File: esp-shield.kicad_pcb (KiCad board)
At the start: 2 copper layers, 53.5 x 52.5 mm, 23 parts, among them J1 Conn_02x03_Counter_Clockwise, J2 Conn_01x08, J3 Conn_01x06, J4 Conn_01x08, SW1 RESET, SW2 PROG, U2 ESP-01

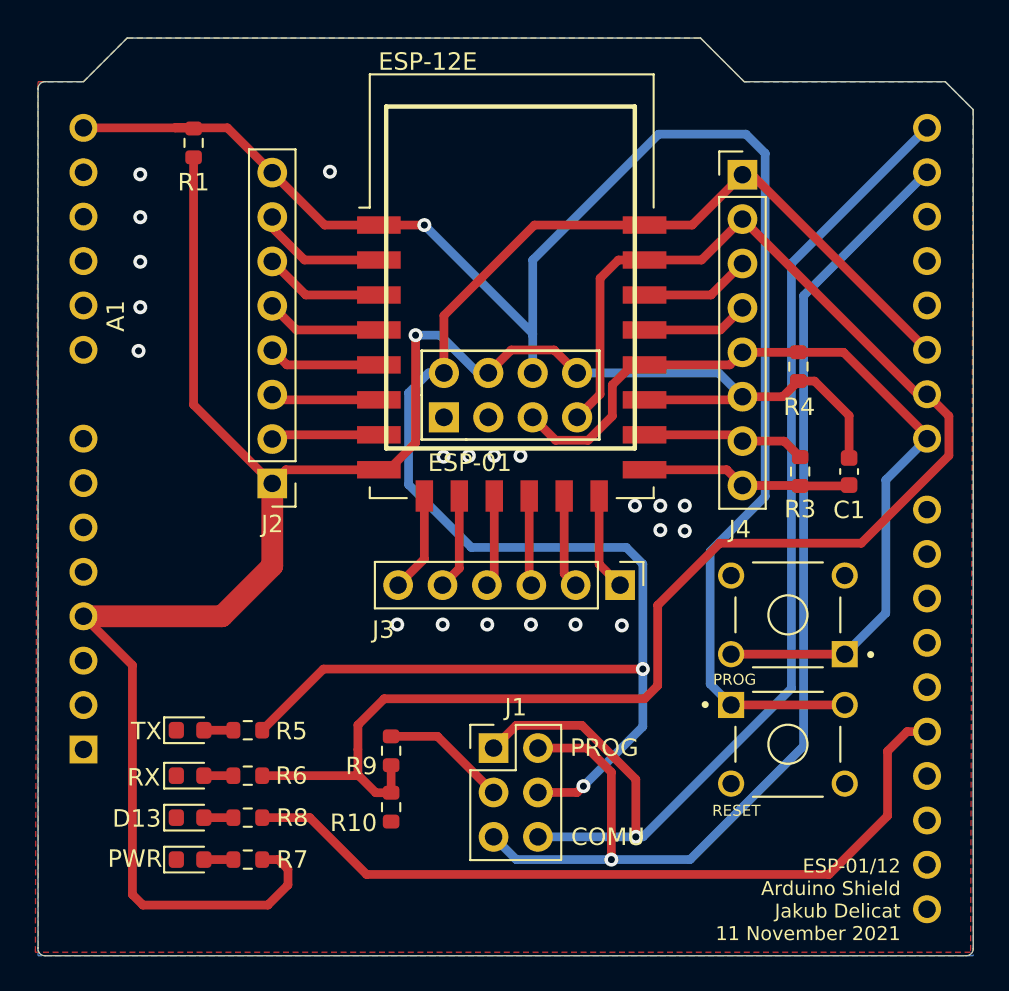
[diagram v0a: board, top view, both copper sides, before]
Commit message: Added esp112E labeling
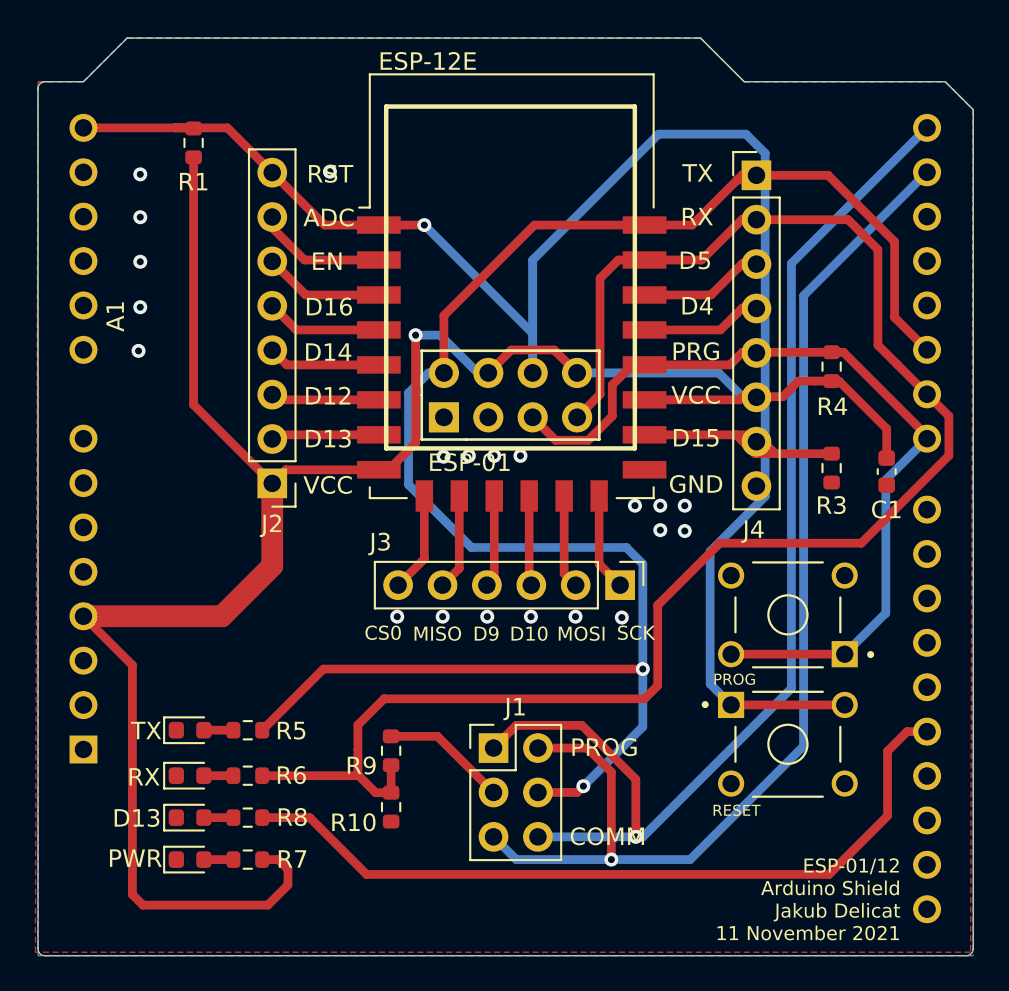
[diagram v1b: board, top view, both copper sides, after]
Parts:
- moved C1 2.15 mm to (101.0, 44.5)
- moved R4 1.90 mm to (97.8, 38.5)
- moved R3 1.81 mm to (97.8, 44.3)
- moved J4 0.80 mm to (93.5, 27.6)
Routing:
- net GND: track 12.1 -> 0.21 mm
- net GPIO15: track 9.43 -> 13.9 mm
- net RX_PROG: track 91.9 -> 95.9 mm
- net TX_PROG: track 101.7 -> 105.2 mm
- net VCC: track 118.5 -> 120.7 mm
- net GPIO4: track 6.12 -> 6.94 mm
- net GPIO5: track 6.35 -> 7.16 mm
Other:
- board text added: "ADC"
- board text added: "COMM"
- board text added: "CS0"
- board text added: "D10"
- board text added: "D12"
- board text added: "D13"
- board text added: "D14"
- board text added: "D15"
- board text added: "D16"
- board text added: "D4"
- board text added: "D5"
- board text added: "D9"
- board text added: "EN"
- board text added: "GND"
- board text added: "MISO"
- board text added: "MOSI"
- board text added: "PRG"
- board text added: "RST"
- board text added: "RX"
- board text added: "SCK"
- board text added: "TX"
- board text added: "VCC"
- board text removed: "COMU"

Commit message: Added Arduino pinout labels
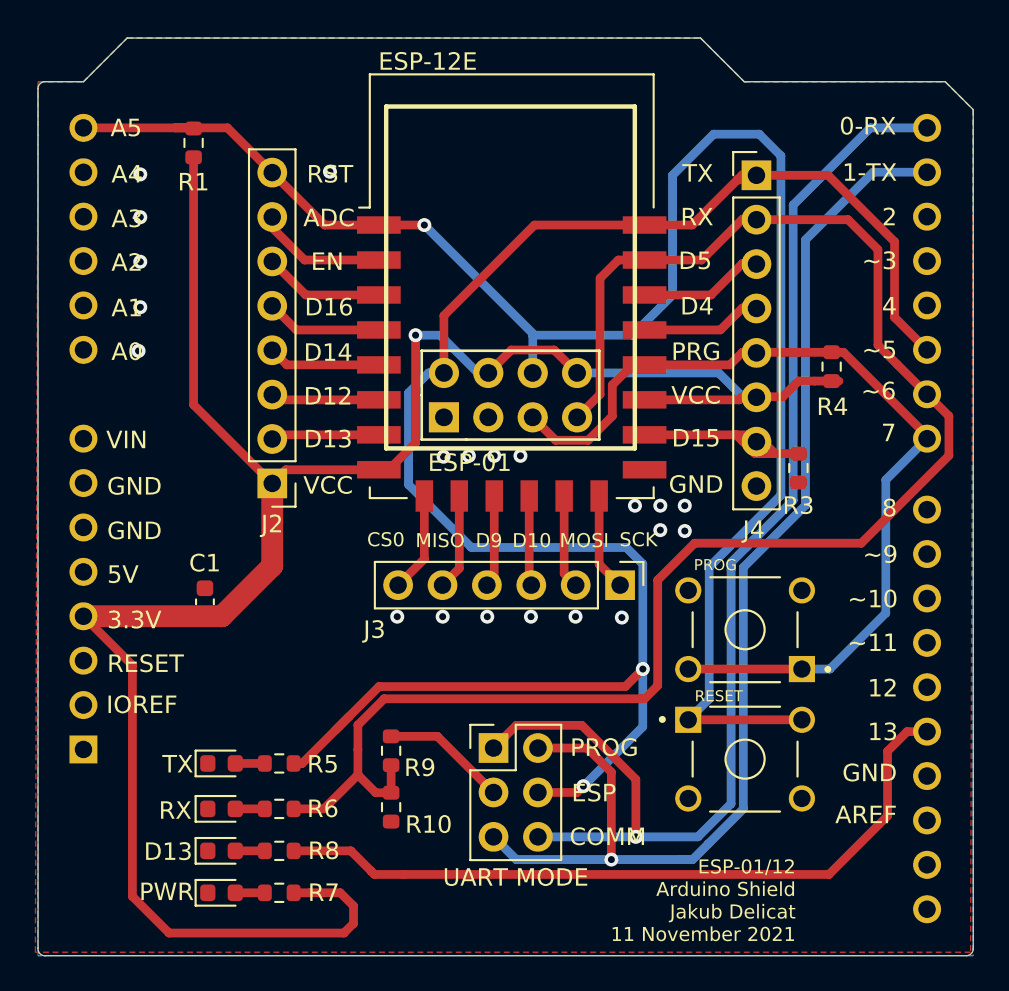
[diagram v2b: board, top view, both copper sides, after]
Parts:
- J1: value Conn_02x03_Counter_Clockwise -> UART MODE
- moved C1 39.7 mm to (62.0, 52.0), turned to 90 degrees
- moved BUILTIN1 2.62 mm to (62.9, 66.2)
- moved D1 2.62 mm to (62.9, 61.2)
- moved R5 2.62 mm to (66.2, 61.2)
- moved R8 2.62 mm to (66.2, 66.2)
- moved R6 2.62 mm to (66.2, 63.8)
- moved RX1 2.62 mm to (62.9, 63.8)
- moved PWR1 2.62 mm to (62.9, 68.6)
- moved R7 2.62 mm to (66.2, 68.6)
- moved SW1 2.59 mm to (92.8, 61.0)
- moved SW2 2.59 mm to (92.8, 53.5)
- moved R3 1.90 mm to (95.9, 44.3)
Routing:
- net /RX_AR: track 66.6 -> 71.4 mm
- net RST: track 94.8 -> 98.4 mm
- net PROG: track 49.5 -> 52.3 mm
- net D13: track 44.9 -> 42.3 mm
- net /TX_AR: track 66.5 -> 68.9 mm
- net GPIO15: track 13.9 -> 12.0 mm
- net VCC: track 120.7 -> 121.6 mm
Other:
- board text added: "0-RX"
- board text added: "1-TX"
- board text added: "12"
- board text added: "13"
- board text added: "2"
- board text added: "3.3V"
- board text added: "4"
- board text added: "5V"
- board text added: "7"
- board text added: "8"
- board text added: "A0"
- board text added: "A1"
- board text added: "A2"
- board text added: "A3"
- board text added: "A4"
- board text added: "A5"
- board text added: "AREF"
- board text added: "ESP"
- board text added: "IOREF"
- board text added: "RESET"
- board text added: "VIN"
- board text added: "~~10"
- board text added: "~~11"
- board text added: "~~3"
- board text added: "~~5"
- board text added: "~~6"
- board text added: "~~9"

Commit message: FLipped arduino xD
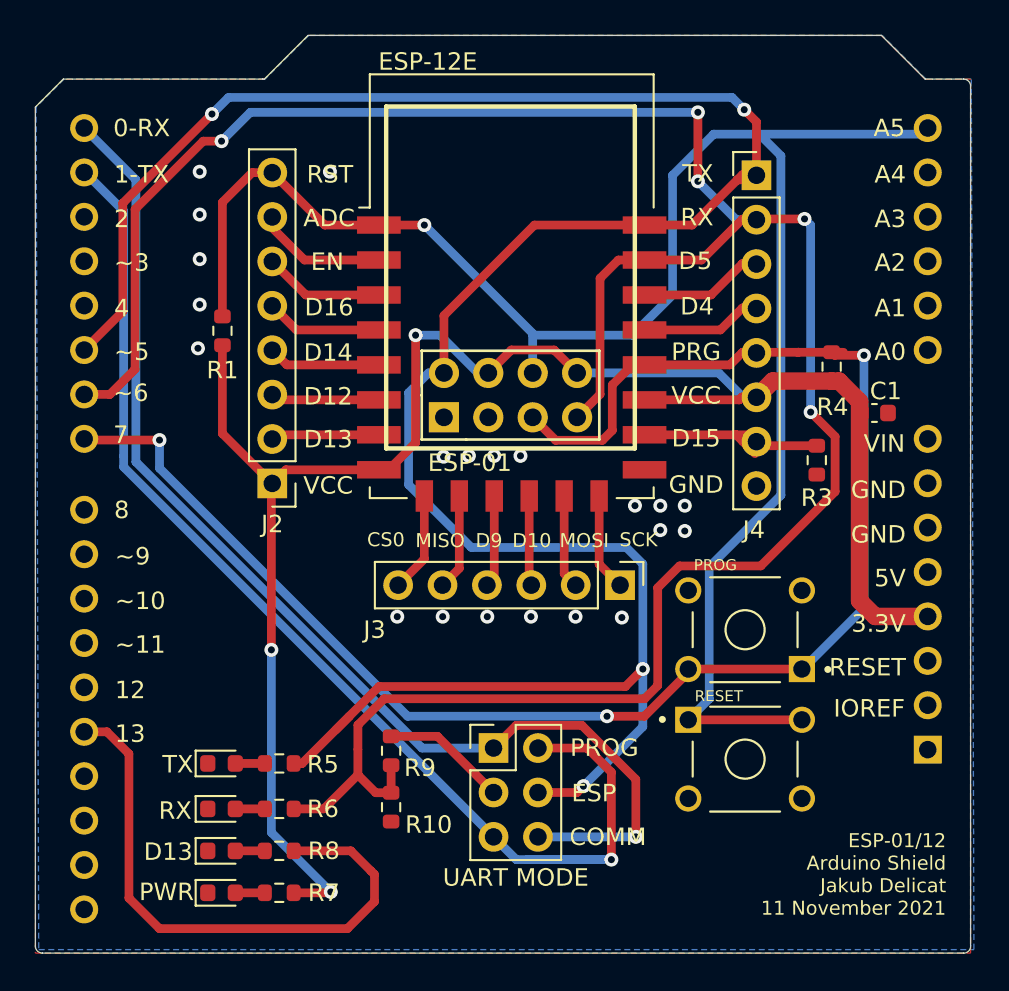
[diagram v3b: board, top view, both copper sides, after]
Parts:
- A1: moved to B.Cu
- moved A1 48.3 mm to (103.3, 60.4)
- moved C1 39.8 mm to (100.2, 41.1), turned to 0 degrees
- moved R1 10.9 mm to (63.0, 36.5)
- moved R3 1.14 mm to (97.0, 43.9)
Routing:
- net RX_PROG: track 95.7 -> 140.8 mm, vias 0 -> 5
- net PROG: track 52.3 -> 93.5 mm, vias 0 -> 3
- net TX_PROG: track 105.3 -> 140.4 mm, vias 2 -> 4
- net VCC: track 121.6 -> 102.8 mm, vias 1 -> 3
- net D13: track 42.3 -> 33.5 mm
- net RST: track 98.4 -> 105.3 mm
- net /RX_AR: track 71.4 -> 66.4 mm
- net /TX_AR: track 68.9 -> 69.6 mm
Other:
- outline, holes or cut-outs redrawn
- board text removed: "AREF"

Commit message: ADDED JP ASD
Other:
- board text added: "JBLJBLJBLBJL"
